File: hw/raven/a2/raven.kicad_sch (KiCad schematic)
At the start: 79 parts, among them J101 Pinhdr_01x02, J102 Pinhdr_01x03, J103 JTAG IN, J104 Pinhdr_01x03, J105 Pinhdr_01x03, SW101 SW_Push, U101 74LS148, U102 74AHC157, U103 SN74LVCH16245, U104 MC68150, U105 CY2308, U106 SN74LVCH16245, U107 MC68060, U108 ATF1508, X101 48Mhz (3.3V)

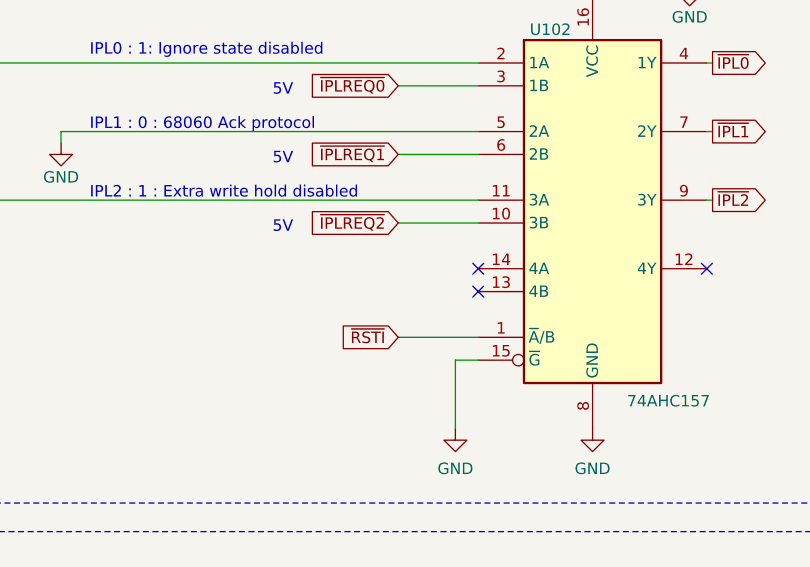
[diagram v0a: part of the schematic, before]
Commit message: minor fixes
- replace IDE header footprint and part
- fix floating (unused) inputs on U102
- removed ckbd debug pads
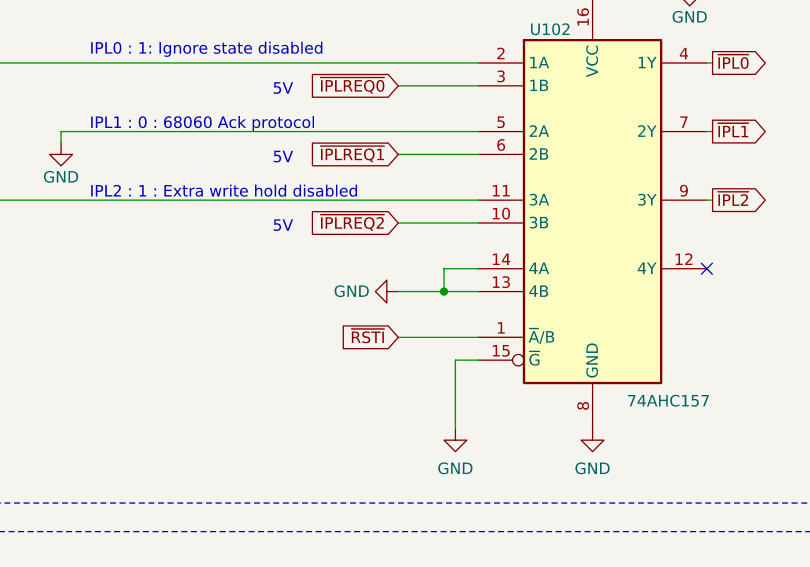
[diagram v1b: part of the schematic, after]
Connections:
- net GND: now also U102.13 (4B), U102.14 (4A)
- no-connect marks 30 -> 28
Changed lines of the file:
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@@
 	)
 	(junction
+		(at 415.29 71.755)
+		(diameter 0)
+		(color 0 0 0 0)
+	)
+	(junction
 		(at 234.315 216.535)
 		(diameter 0)
@@
 	)
 	(no_connect
-		(at 419.1 69.215)
-	)
-	(no_connect
 		(at 180.34 349.25)
 	)
@@
 	)
 	(no_connect
-		(at 419.1 71.755)
-	)
-	(no_connect
 		(at 180.34 339.09)
 	)
@@
 	(wire
 		(pts
+			(xy 415.29 69.215) (xy 415.29 71.755)
+		)
+		(stroke
+			(width 0)
+			(type default)
+		)
+	)
+	(wire
+		(pts
 			(xy 718.185 185.42) (xy 721.995 185.42)
 		)
@@
 	(wire
 		(pts
+			(xy 415.29 71.755) (xy 419.1 71.755)
+		)
+		(stroke
+			(width 0)
+			(type default)
+		)
+	)
+	(wire
+		(pts
 			(xy 657.225 305.435) (xy 657.225 306.705)
 		)
@@
 		)
 	)
+	(wire
+		(pts
+			(xy 419.1 69.215) (xy 415.29 69.215)
+		)
+		(stroke
+			(width 0)
+			(type default)
+		)
+	)
 	(bus
 		(pts
@@
 	(wire
 		(pts
+			(xy 410.21 71.755) (xy 415.29 71.755)
+		)
+		(stroke
+			(width 0)
+			(type default)
+		)
+	)
+	(wire
+		(pts
 			(xy 286.385 216.535) (xy 283.845 216.535)
 		)
@@
 					(unit 1)
 				)
+			)
+		)
+	)
+	(symbol
+		(lib_id "power:GND")
+		(at 410.21 71.755 270)
+		(unit 1)
+		(exclude_from_sim no)
+		(in_bom yes)
+		(on_board yes)
+		(dnp no)
+		(property "Reference" "#PWR0165"
+			(at 403.86 71.755 0)
+			(effects
+				(font
+					(size 1.27 1.27)
+				)
+				(hide yes)
+			)
+		)
+		(property "Value" "GND"
+			(at 407.035 71.755 90)
+			(effects
+				(font
+					(size 1.27 1.27)
+				)
+				(justify right)
+			)
+		)
+		(property "Footprint" ""
+			(at 410.21 71.755 0)
+			(effects
+				(font
+					(size 1.27 1.27)
+				)
+				(hide yes)
+			)
+		)
+		(property "Datasheet" ""
+			(at 410.21 71.755 0)
+			(effects
+				(font
+					(size 1.27 1.27)
+				)
+				(hide yes)
+			)
+		)
+		(property "Description" ""
+			(at 410.21 71.755 0)
+			(effects
+				(font
+					(size 1.27 1.27)
+				)
+			)
+		)
+		(pin "1"
+		)
+		(instances
+			(project "raven"
+				(path "/af55e73e-5814-45b4-ac5c-0bab62c0b1c7"
+					(reference "#PWR0165")
+					(unit 1)
+				)

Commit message: A2 rework
- reworking top-left area for dsp56303
- internal speaker header for YM
- software controlled volume for YM
- misc routing cleanup
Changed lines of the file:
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@@
 	(title_block
 		(title "Raven 68060")
-		(date "2025")
+		(date "2026")
 		(rev "A2")
 		(company "Licensed under CERN-OHL-W v2")
-		(comment 1 "(c)2025 Anders Granlund")
+		(comment 1 "(c)2026 Anders Granlund")
 	)
 	(rectangle
@@
 			)
 			(justify left top)
+		)
+	)
+	(text_box "todo:\nremove header and clean up routing"
+		(exclude_from_sim no)
+		(at 180.34 119.38 0)
+		(size 48.895 13.335)
+		(margins 0.9525 0.9525 0.9525 0.9525)
+		(stroke
+			(width 0)
+			(type solid)
+		)
+		(fill
+			(type color)
+			(color 255 230 63 0.53)
+		)
+		(effects
+			(font
+				(size 1.27 1.27)
+				(color 0 0 0 1)
+			)
+			(justify left top)

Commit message: A2: DSP ram routing
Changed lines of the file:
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@@
 			(font
 				(size 3 3)
+				(thickness 0.6)
+				(bold yes)
 			)
 			(justify left bottom)
@@
 			(font
 				(size 3 3)
+				(thickness 0.6)
+				(bold yes)
 			)
 			(justify left bottom)
@@
 			(font
 				(size 3 3)
+				(thickness 0.6)
+				(bold yes)
 			)
 			(justify left bottom)
@@
 			(font
 				(size 3 3)
+				(thickness 0.6)
+				(bold yes)
 			)
 			(justify left bottom)
@@
 			(font
 				(size 3 3)
+				(thickness 0.6)
+				(bold yes)
 			)
 			(justify left bottom)
@@
 			(font
 				(size 3 3)
+				(thickness 0.6)
+				(bold yes)
 			)
 			(justify left bottom)
@@
 			(font
 				(size 3 3)
+				(thickness 0.6)
+				(bold yes)
 			)
 			(justify left bottom)
@@
 			(font
 				(size 3 3)
+				(thickness 0.6)
+				(bold yes)
 			)
 			(justify left bottom)
@@
 			(font
 				(size 3 3)
+				(thickness 0.6)
+				(bold yes)
 			)
 			(justify left bottom)

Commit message: A2 wip
audio hooked up
added caps for fan headers
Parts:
- added C105, C106: 1u, Capacitor_SMD:C_1206_3216Metric_Pad1.33x1.80mm_HandSolder, symbol 68k:c_100nf_smd1206
- renumbered C105 to C107, C106 to C108, C107 to C109, C108 to C110, C109 to C111, C110 to C112, C111 to C113, C112 to C114, C113 to C115, C114 to C116, C115 to C117, C116 to C118, C117 to C119, C118 to C120, C119 to C121, C120 to C122, C121 to C123, C122 to C124, C123 to C125, C124 to C126, C125 to C127, C126 to C128, C127 to C129, C128 to C130
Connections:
- net +5V: now also C105.2, C106.2
- net GND: now also C105.1, C106.1

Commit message: misc a2 work
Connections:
- net ~{ETH_CS} is gone; now on net ~{UART_CS}: U108.81 (GCLK3/IOH)
- net ~{IRQ_MFP}: now also U101.3 (I6); no longer U101.2 (I5)
- net ~{IRQ_UART}: now also U101.2 (I5); no longer U101.3 (I6)
- net ~{UART_CS}: no longer U108.80 (IOH)
- net ~{IRQ_VBL}: now reaches R104.2, U101.1 (I4)
- new net ~{DSP_CS}: U108.80 (IOH)
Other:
- moved on the sheet: R120
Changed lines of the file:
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@@
 	(text_box "68060UM + Errata:\n\nTHERM1 and THERM0 are connected to an internal thermal resistor\nand provide information about the average temperature of the die.\n\nThe resistance across these two pins is proportional to the average\ntemperature of the die.\n\nThe temperature coefficient of the resistor is approximately\n2.8 Ω/°C with a nominal resistance of 780 ohm at 25°C.\n"
 		(exclude_from_sim no)
-		(at 325.12 411.48 0)
-		(size 62.865 17.78)
+		(at 321.945 398.78 0)
+		(size 55.245 17.78)
 		(margins 0.75 0.75 0.75 0.75)
 		(stroke
@@
 		)
 	)
-	(text_box "Changes from rev.A1:\n\n- pin34 is now A6 instead of A5\n- pin73 is now /BUSCS instead of unused header\n- pin81 is now /ETH_CS instead of unused header\n- pin54 is wire-or of /ISA:IOCS16 and /ISA:MEMCS16"
+	(text_box "Changes from rev.A1:\n\n- pin34 is now A6 instead of A5\n- pin73 is now /BUSCS instead of unused header\n- pin80 is now /DSP_CS instead of /UART_CS\n- pin81 is now /UART_CS instead of unused header\n- pin54 is wire-or of /ISA:IOCS16 and /ISA:MEMCS16"
 		(exclude_from_sim no)
 		(at 522.605 308.61 0)
-		(size 59.69 16.51)
+		(size 59.69 30.48)
 		(margins 0.9525 0.9525 0.9525 0.9525)
 		(stroke
@@
 	)
 	(junction
+		(at 347.98 396.24)
+		(diameter 0)
+		(color 0 0 0 0)
+	)
+	(junction
 		(at 247.015 216.535)
 		(diameter 0)
@@
 	)
 	(junction
-		(at 315.595 396.24)
-		(diameter 0)
-		(color 0 0 0 0)
-	)
-	(junction
 		(at 407.67 120.015)
 		(diameter 0)
@@
 	)
 	(junction
+		(at 248.92 63.5)
+		(diameter 0)
+		(color 0 0 0 0)
+	)
+	(junction
 		(at 47.625 537.845)
 		(diameter 0)
@@
 	)
 	(junction
+		(at 253.365 58.42)
+		(diameter 0)
+		(color 0 0 0 0)
+	)
+	(junction
 		(at 570.865 68.58)
 		(diameter 0)
@@
 	)
 	(junction
-		(at 248.92 60.96)
-		(diameter 0)
-		(color 0 0 0 0)
-	)
-	(junction
 		(at 92.71 530.225)
 		(diameter 0)
@@
 	(wire
 		(pts
-			(xy 216.535 63.5) (xy 279.4 63.5)
+			(xy 216.535 63.5) (xy 248.92 63.5)
 		)
 		(stroke
@@
 	(wire
 		(pts
-			(xy 313.055 396.24) (xy 315.595 396.24)
-		)
-		(stroke
-			(width 0)
-			(type default)
-		)
-	)
-	(wire
-		(pts
 			(xy 635.635 424.815) (xy 635.635 426.085)
 		)
@@
 	(wire
 		(pts
-			(xy 216.535 60.96) (xy 248.92 60.96)
+			(xy 216.535 60.96) (xy 279.4 60.96)
 		)
 		(stroke
@@
 		)
 	)
+	(wire
+		(pts
+			(xy 248.92 44.45) (xy 248.92 63.5)
+		)
+		(stroke
+			(width 0)
+			(type default)
+		)
+	)
 	(bus
 		(pts
@@
 	(wire
 		(pts
-			(xy 248.92 60.96) (xy 279.4 60.96)
-		)
-		(stroke
-			(width 0)
-			(type default)
-		)
-	)
-	(wire
-		(pts
 			(xy 109.22 548.005) (xy 118.745 548.005)
 		)
@@
 	(wire
 		(pts
+			(xy 347.98 396.24) (xy 362.585 396.24)
+		)
+		(stroke
+			(width 0)
+			(type default)
+		)
+	)
+	(wire
+		(pts
 			(xy 580.39 124.46) (xy 580.39 126.365)
 		)
@@
 	(wire
 		(pts
+			(xy 248.92 63.5) (xy 279.4 63.5)
+		)
+		(stroke
+			(width 0)
+			(type default)
+		)
+	)
+	(wire
+		(pts
 			(xy 612.14 382.905) (xy 614.045 382.905)
 		)
@@
 	(wire
 		(pts
-			(xy 248.92 44.45) (xy 248.92 60.96)
-		)
-		(stroke
-			(width 0)
-			(type default)
-		)
-	)
-	(wire
-		(pts
 			(xy 198.755 216.535) (xy 198.755 218.44)
 		)
@@
 	(wire
 		(pts
-			(xy 326.39 396.24) (xy 327.66 396.24)
-		)
-		(stroke
-			(width 0)
-			(type default)
-		)
-	)
-	(wire
-		(pts
 			(xy 266.065 407.67) (xy 266.065 410.845)
 		)
@@
 		)
 	)
+	(wire
+		(pts
+			(xy 347.98 394.335) (xy 347.98 396.24)
+		)
+		(stroke
+			(width 0)
+			(type default)
+		)
+	)
 	(bus
 		(pts
@@
 	(wire
 		(pts
-			(xy 315.595 396.24) (xy 318.77 396.24)
+			(xy 313.055 396.24) (xy 347.98 396.24)
 		)
 		(stroke
@@
 	(wire
 		(pts
-			(xy 315.595 400.685) (xy 343.535 400.685)
-		)
-		(stroke
-			(width 0)
-			(type default)
-		)
-	)
-	(wire
-		(pts
 			(xy 208.915 216.535) (xy 208.915 218.44)
 		)
@@
 		)
 	)
+	(wire
+		(pts
+			(xy 216.535 58.42) (xy 253.365 58.42)
+		)
+		(stroke
+			(width 0)
+			(type default)
+		)
+	)
 	(bus
 		(pts
@@
 	(wire
 		(pts
-			(xy 315.595 396.24) (xy 315.595 400.685)
-		)
-		(stroke
-			(width 0)
-			(type default)
-		)
-	)
-	(wire
-		(pts
 			(xy 239.395 216.535) (xy 239.395 218.44)
 		)
@@
 		)
 	)
-	(global_label "~{ETH_CS}"
+	(global_label "~{DSP_CS}"
 		(shape output)
-		(at 670.56 329.565 0)
+		(at 670.56 332.105 0)
 		(fields_autoplaced yes)
 		(effects
@@
 		)
 		(property "Intersheetrefs" "${INTERSHEET_REFS}"
-			(at 680.284 329.565 0)
+			(at 680.5816 332.105 0)
 			(effects
 				(font
@@
 	(global_label "~{IRQ_UART}"
 		(shape input)
-		(at 216.535 63.5 180)
+		(at 216.535 60.96 180)
 		(fields_autoplaced yes)
 		(effects
@@
 		)
 		(property "Intersheetrefs" "${INTERSHEET_REFS}"
-			(at 204.7202 63.5 0)
+			(at 204.7202 60.96 0)
 			(effects
 				(font
@@
 	(global_label "TEMP2"
 		(shape output)
-		(at 343.535 400.685 0)
+		(at 362.585 396.24 0)
 		(fields_autoplaced yes)
 		(effects
@@
 		)
 		(property "Intersheetrefs" "${INTERSHEET_REFS}"
-			(at 350.6473 400.685 0)
+			(at 369.6973 396.24 0)
 			(effects
 				(font
@@
 	(global_label "~{IRQ_MFP}"
 		(shape input)
-		(at 216.535 60.96 180)
+		(at 216.535 63.5 180)
 		(fields_autoplaced yes)
 		(effects
@@
 		)
 		(property "Intersheetrefs" "${INTERSHEET_REFS}"
-			(at 205.5669 60.96 0)
+			(at 205.5669 63.5 0)
 			(effects
 				(font
@@
 	(global_label "~{UART_CS}"
 		(shape output)
-		(at 670.56 332.105 0)
+		(at 670.56 329.565 0)
 		(fields_autoplaced yes)
 		(effects
@@
 		)
 		(property "Intersheetrefs" "${INTERSHEET_REFS}"
-			(at 681.649 332.105 0)
+			(at 681.649 329.565 0)
 			(effects
 				(font
@@
 		)
 	)
+	(global_label "~{IRQ_VBL}"
+		(shape input)
+		(at 216.535 58.42 180)
+		(fields_autoplaced yes)
+		(effects
+			(font
+				(size 1.27 1.27)
+			)
+			(justify right)
+		)
+		(property "Intersheetrefs" "${INTERSHEET_REFS}"
+			(at 205.9902 58.42 0)
+			(effects
+				(font
+					(size 1.27 1.27)
+				)
+				(justify right)
+				(hide yes)
+			)
+		)
+	)
 	(global_label "~{IPLREQ1}"
 		(shape output)
@@
 	(symbol
 		(lib_id "power:+3.3V")
-		(at 327.66 396.24 270)
+		(at 347.98 386.715 0)
 		(unit 1)
 		(exclude_from_sim no)
@@
 		(on_board yes)
 		(dnp no)
-		(property "Reference" "#PWR0149"
-			(at 323.85 396.24 0)
+		(property "Reference" "#PWR0147"
+			(at 347.98 390.525 0)
 			(effects
 				(font
@@
 		)
 		(property "Value" "+3.3V"
-			(at 333.756 396.24 90)
+			(at 347.853 382.778 0)
 			(effects
 				(font
@@
 		)
 		(property "Footprint" ""
-			(at 327.66 396.24 0)
+			(at 347.98 386.715 0)
 			(effects
 				(font
@@
 		)
 		(property "Datasheet" ""
-			(at 327.66 396.24 0)
+			(at 347.98 386.715 0)
 			(effects
 				(font
@@
 		)
 		(property "Description" ""
-			(at 327.66 396.24 0)
+			(at 347.98 386.715 0)
 			(effects
 				(font
@@
 			(project "raven"
 				(path "/af55e73e-5814-45b4-ac5c-0bab62c0b1c7"
-					(reference "#PWR0149")
+					(reference "#PWR0147")
 					(unit 1)
 				)
@@
 		(on_board yes)
 		(dnp no)
-		(property "Reference" "#PWR0148"
+		(property "Reference" "#PWR0149"
 			(at 334.01 393.7 0)
 			(effects
@@
 			(project "raven"
 				(path "/af55e73e-5814-45b4-ac5c-0bab62c0b1c7"
-					(reference "#PWR0148")
+					(reference "#PWR0149")
 					(unit 1)
 				)
@@
 	(symbol
 		(lib_id "Device:R")
-		(at 322.58 396.24 270)
+		(at 347.98 390.525 0)
 		(unit 1)
 		(exclude_from_sim no)
@@
 		(dnp no)
 		(property "Reference" "R120"
-			(at 320.04 396.24 90)
+			(at 347.98 393.065 90)
 			(effects
 				(font
@@
 		)
 		(property "Value" "1K"
-			(at 321.31 398.145 90)
+			(at 349.885 391.795 90)
 			(effects
 				(font
@@
 		)
 		(property "Footprint" "Resistor_SMD:R_1206_3216Metric_Pad1.30x1.75mm_HandSolder"
-			(at 322.58 394.462 90)
+			(at 346.202 390.525 90)
 			(effects
 				(font
@@
 		)
 		(property "Datasheet" "~"
-			(at 322.58 396.24 0)
+			(at 347.98 390.525 0)
 			(effects
 				(font
@@
 		)
 		(property "Description" ""
-			(at 322.58 396.24 0)
+			(at 347.98 390.525 0)
 			(effects
 				(font
@@
 		)
 		(property "Manufacturer_Name" "Yageo"
-			(at 322.58 396.24 0)
+			(at 347.98 390.525 0)
 			(effects
 				(font
@@
 		)
 		(property "Manufacturer_Part_Number" "RT1206FRE071KL"
-			(at 322.58 396.24 0)
+			(at 347.98 390.525 0)
 			(effects
 				(font
@@
 		(on_board yes)
 		(dnp no)
-		(property "Reference" "#PWR0147"
+		(property "Reference" "#PWR0148"
 			(at 320.04 389.89 0)
 			(effects
@@
 			(project "raven"
 				(path "/af55e73e-5814-45b4-ac5c-0bab62c0b1c7"
-					(reference "#PWR0147")
+					(reference "#PWR0148")
 					(unit 1)
 				)

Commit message: A2 routing
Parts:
- removed J102: Pinhdr_01x03, Connector_PinHeader_2.54mm:PinHeader_1x03_P2.54mm_Vertical, symbol Connector_Generic:Conn_01x03
- removed R101, R123, R124: 10K, Resistor_SMD:R_1206_3216Metric_Pad1.30x1.75mm_HandSolder, symbol Device:R
- renumbered J103 to J102, J104 to J103, J105 to J104, R102 to R101, R103 to R102, R104 to R103, R105 to R104, R106 to R105, R112 to R106, R108 to R107, R109 to R108, R110 to R109, R111 to R110, R116 to R111, R107 to R112, R117 to R116, R118 to R117, R119 to R118, R120 to R119, R121 to R120, R122 to R121
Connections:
- net PCLK_X2 is gone; now on an unnamed net: U105.2 (CLKA1)
- net ~{CDIS} is gone; now on net +3.3V: U107.T05 (~{CDIS})
- net ~{MDIS} is gone; now on net +3.3V: U107.S06 (~{MDIS})
- net +3.3V: now also J104.3 (Pin_3), U102.11 (3A), U102.2 (1A); no longer R111.1
- net GND: now also J104.1 (Pin_1)
- net at J104.2 (Pin_2): now also R111.2
- net PCLK_X1: no longer names the net of U105.6 (CLKB1)
- net ~{CPUX2}: no longer names the net of U108.10 (IOA)
- net ~{CPUX2}: no longer J103.2 (Pin_2)
- net ~{JTAG_RESET} renamed ~{ATF_OE1}
- net ~{ATF_OE1}: now also R111.1
- no-connect marks 28 -> 31
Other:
- note added: "Generic options header for OE1 pin. 1:2 = lo 3:2 = hi Put 12V on pin2 to unlock jtag if chip was programmed with jtag disabled."
- moved on the sheet: J103, J104, R106, R111, R112

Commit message: A2: schema + routing complete. ERC + DRC complete.
Let sit for a while, revisit and sanity check with fresh eyes before gerber.
Todo: double check BOM export and fix missing infos if any.
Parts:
- removed J103: Pinhdr_01x03, Connector_PinHeader_2.54mm:PinHeader_1x03_P2.54mm_Vertical, symbol Connector_Generic:Conn_01x03
- removed R103, R104, R105, R106: 10K, Resistor_SMD:R_1206_3216Metric_Pad1.30x1.75mm_HandSolder, symbol Device:R
- renumbered J104 to J103, R107 to R103, R108 to R104, R109 to R105, R110 to R106, R112 to R107, R113 to R108, R114 to R109, R115 to R110, R116 to R112, R117 to R113, R118 to R114, R119 to R115, R120 to R116, R121 to R117
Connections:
- net ~{IRQ_VBL} is gone; now on net +5V: U101.1 (I4)
- net +5V: now also U101.10 (IO), U101.11 (I1), U101.12 (I2), U101.13 (I3)
- net ~{IRQ_NMI}: now reaches J101.2 (Pin_2), R101.2, SW101.2, U101.4 (I7)
- no-connect marks 31 -> 30
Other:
- note added: "Generic jumper header for OE1 pin. 1:2 = lo 3:2 = hi Can also put 12V on pin2 to unlock jtag if chip was programmed with jtag disabled."
- note added: "spare"
- note removed: "Generic options header for OE1 pin. 1:2 = lo 3:2 = hi Put 12V on pin2 to unlock jtag if chip was programmed with jtag disabled."
- moved on the sheet: J103, R101, R102, R111
